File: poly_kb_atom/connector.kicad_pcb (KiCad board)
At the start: 2 copper layers, 15.9 x 119 mm, 36 parts, among them J1 Conn_01x09, J10 Conn_01x09, J11 Conn_01x09, J12 Conn_01x09, J13 Conn_01x07, J14 Conn_01x06, J15 Conn_01x01, J16 Conn_01x02, J17 Conn_01x01, J2 Conn_01x09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

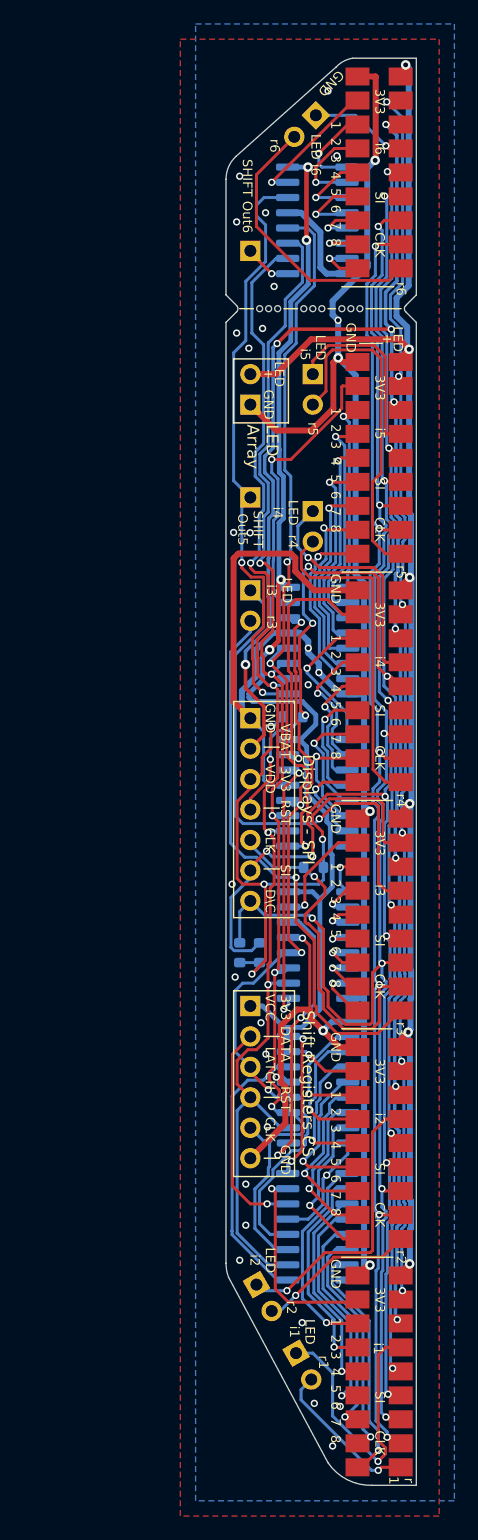
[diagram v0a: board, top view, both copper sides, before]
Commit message: Fixed wrong connection in between pin 16 an VCC in PolyAtom2; Added ConectorL
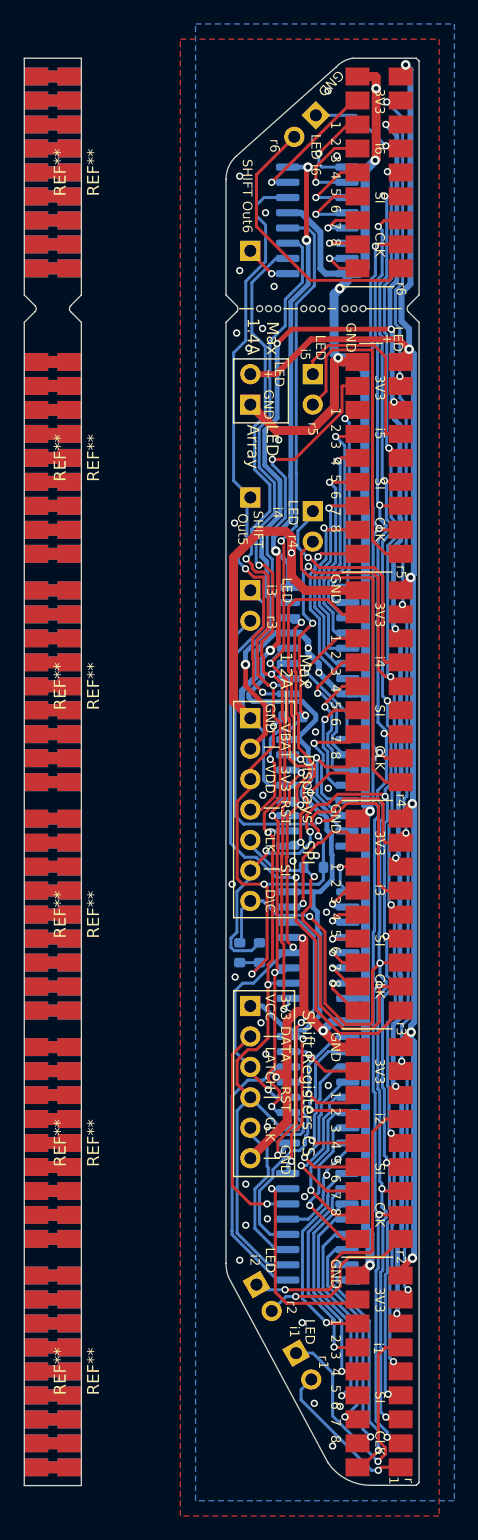
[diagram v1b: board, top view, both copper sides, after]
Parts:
- added REF**: AtomConnect2, poly_kb:AtomConnect2, F.Cu at (62.9, 120.0)
- added REF**: AtomConnect2, poly_kb:AtomConnect2, F.Cu at (65.7, 39.1)
- added REF**: AtomConnect2, poly_kb:AtomConnect2, F.Cu at (65.7, 81.9)
- added REF**: AtomConnect2, poly_kb:AtomConnect2, F.Cu at (65.7, 62.9)
- added REF**: AtomConnect2, poly_kb:AtomConnect2, B.Cu at (65.7, 139.1)
- added REF**: AtomConnect2, poly_kb:AtomConnect2, B.Cu at (65.7, 120.0)
- added REF**: AtomConnect2, poly_kb:AtomConnect2, B.Cu at (65.7, 101.0)
- added REF**: AtomConnect2, poly_kb:AtomConnect2, B.Cu at (65.7, 39.1)
- added REF**: AtomConnect2, poly_kb:AtomConnect2, B.Cu at (65.7, 81.9)
- added REF**: AtomConnect2, poly_kb:AtomConnect2, B.Cu at (65.7, 62.9)
- added REF**: AtomConnect2, poly_kb:AtomConnect2, B.Cu at (62.9, 139.1)
- added REF**: AtomConnect2, poly_kb:AtomConnect2, F.Cu at (65.7, 139.1)
- added REF**: AtomConnect2, poly_kb:AtomConnect2, B.Cu at (62.9, 120.0)
- added REF**: AtomConnect2, poly_kb:AtomConnect2, B.Cu at (62.9, 101.0)
- added REF**: AtomConnect2, poly_kb:AtomConnect2, B.Cu at (62.9, 81.9)
- added REF**: AtomConnect2, poly_kb:AtomConnect2, B.Cu at (62.9, 62.9)
- added REF**: AtomConnect2, poly_kb:AtomConnect2, B.Cu at (62.9, 39.1)
- added REF**: AtomConnect2, poly_kb:AtomConnect2, F.Cu at (62.9, 139.1)
- added REF**: AtomConnect2, poly_kb:AtomConnect2, F.Cu at (62.9, 39.1)
- added REF**: AtomConnect2, poly_kb:AtomConnect2, F.Cu at (62.9, 62.9)
- added REF**: AtomConnect2, poly_kb:AtomConnect2, F.Cu at (62.9, 101.0)
- added REF**: AtomConnect2, poly_kb:AtomConnect2, F.Cu at (62.9, 81.9)
- added REF**: AtomConnect2, poly_kb:AtomConnect2, F.Cu at (65.7, 120.0)
- added REF**: AtomConnect2, poly_kb:AtomConnect2, F.Cu at (65.7, 101.0)
- moved mouse-bite-2mm-slot 0.25 mm to (89.4, 50.4)
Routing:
- net (no net): track 0.00 -> 300.4 mm, vias 1 -> 0
- net +3V3: track 108.2 -> 111.6 mm
- net GND: track 236.1 -> 238.8 mm, vias 35 -> 47
- net 17: track 9.39 -> 10.9 mm
- net SI: track 138.1 -> 136.8 mm
- net 32: track 8.46 -> 9.61 mm
- net LedIn2: track 24.0 -> 25.1 mm
- net VBAT: track 154.3 -> 155.4 mm
- net 33: track 24.5 -> 25.6 mm
- net r2: track 13.2 -> 14.2 mm
- net SHIFTR_RST: track 104.9 -> 105.9 mm
- net 30: track 10.0 -> 10.8 mm
- net SHIFTR_LATCH_CLK: track 105.3 -> 104.6 mm
- net CLK: track 141.4 -> 140.8 mm
- net 31: track 9.71 -> 10.4 mm
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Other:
- board size 15.9 x 119 mm -> 32.9 x 119.1 mm
- board text added: "JLCJLCJLCJLC"
- board text added: "Max 1.2A"
- board text added: "Max 1.4A"
